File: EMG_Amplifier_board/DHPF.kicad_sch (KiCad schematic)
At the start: 7 parts, among them U4 TLV8542DR

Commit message: add footprints
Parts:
- C1, C2: footprint (none) -> Capacitor_SMD:C_0805_2012Metric
- R6, R7, R8, R9: footprint (none) -> Capacitor_SMD:C_0201_0603Metric
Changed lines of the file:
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@@
 			)
 		)
-		(property "Footprint" ""
+		(property "Footprint" "Capacitor_SMD:C_0201_0603Metric"
 			(at 116.332 101.6 90)
 			(effects
@@
 			)
 		)
-		(property "Footprint" ""
+		(property "Footprint" "Capacitor_SMD:C_0805_2012Metric"
 			(at 113.03 62.5348 0)
 			(effects
@@
 			)
 		)
-		(property "Footprint" ""
+		(property "Footprint" "Capacitor_SMD:C_0201_0603Metric"
 			(at 97.282 101.6 90)
 			(effects
@@
 			)
 		)
-		(property "Footprint" ""
+		(property "Footprint" "Capacitor_SMD:C_0805_2012Metric"
 			(at 113.03 113.3348 0)
 			(effects
@@
 			)
 		)
-		(property "Footprint" ""
+		(property "Footprint" "Capacitor_SMD:C_0201_0603Metric"
 			(at 97.282 74.93 90)
 			(effects
@@
 			)
 		)
-		(property "Footprint" ""
+		(property "Footprint" "Capacitor_SMD:C_0201_0603Metric"
 			(at 116.332 74.93 90)
 			(effects

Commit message: acomponents choice
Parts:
- C1, C2: footprint Capacitor_SMD:C_0805_2012Metric -> Capacitor_SMD:C_0603_1608Metric
- R6, R7, R8, R9: footprint Capacitor_SMD:C_0201_0603Metric -> Resistor_SMD:R_0402_1005Metric
- U4: footprint RUG8_TEX -> TLV8542DR_footprints:RUG8_TEX
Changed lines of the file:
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@@
 			)
 		)
-		(property "Footprint" "RUG8_TEX"
+		(property "Footprint" "TLV8542DR_footprints:RUG8_TEX"
 			(at 64.77 66.04 0)
 			(effects
@@
 			)
 		)
-		(property "Footprint" "Capacitor_SMD:C_0201_0603Metric"
+		(property "Footprint" "Resistor_SMD:R_0402_1005Metric"
 			(at 116.332 101.6 90)
 			(effects
@@
 			)
 		)
-		(property "Footprint" "Capacitor_SMD:C_0805_2012Metric"
+		(property "Footprint" "Capacitor_SMD:C_0603_1608Metric"
 			(at 113.03 62.5348 0)
 			(effects
@@
 			)
 		)
-		(property "Footprint" "Capacitor_SMD:C_0201_0603Metric"
+		(property "Footprint" "Resistor_SMD:R_0402_1005Metric"
 			(at 97.282 101.6 90)
 			(effects
@@
 			)
 		)
-		(property "Footprint" "Capacitor_SMD:C_0805_2012Metric"
+		(property "Footprint" "Capacitor_SMD:C_0603_1608Metric"
 			(at 113.03 113.3348 0)
 			(effects
@@
 			)
 		)
-		(property "Footprint" "Capacitor_SMD:C_0201_0603Metric"
+		(property "Footprint" "Resistor_SMD:R_0402_1005Metric"
 			(at 97.282 74.93 90)
 			(effects
@@
 			)
 		)
-		(property "Footprint" "Capacitor_SMD:C_0201_0603Metric"
+		(property "Footprint" "Resistor_SMD:R_0402_1005Metric"
 			(at 116.332 74.93 90)
 			(effects

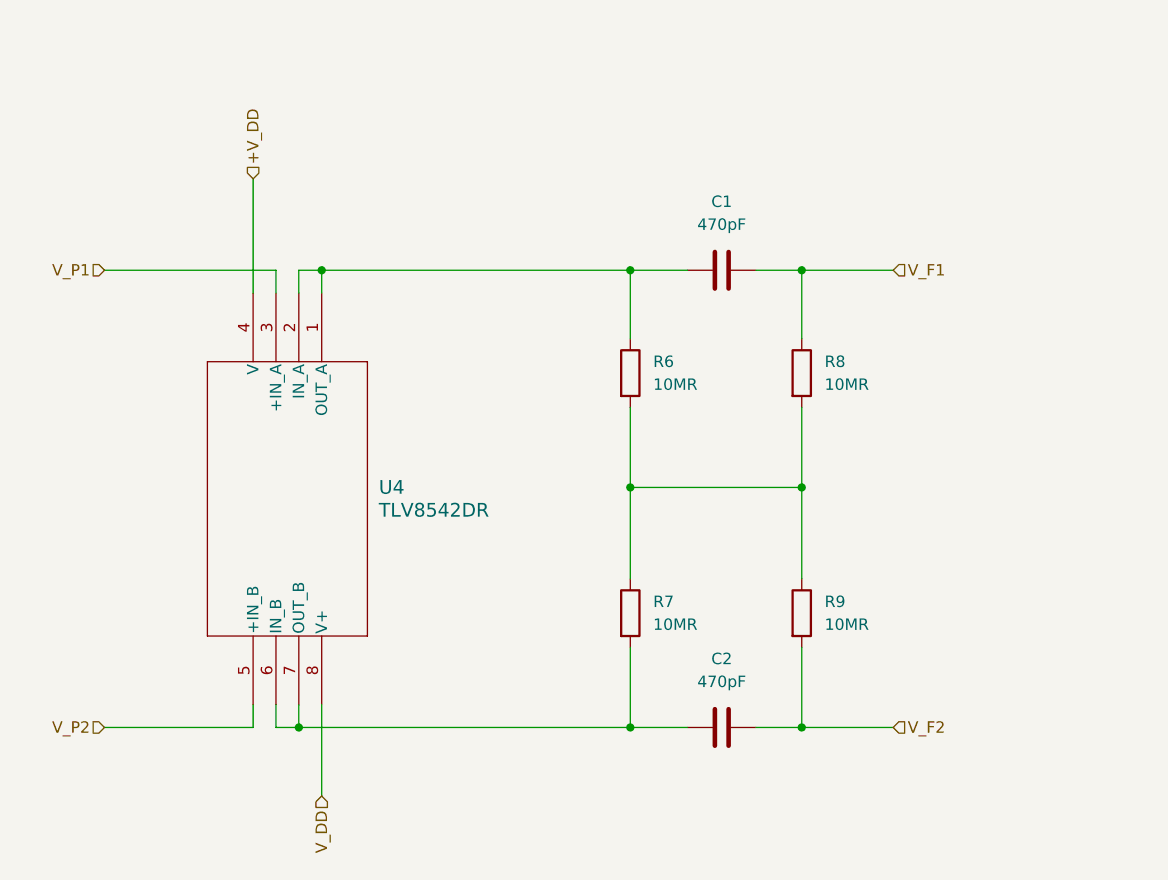
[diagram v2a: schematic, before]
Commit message: update the schematic with shared grounds and pin connectors
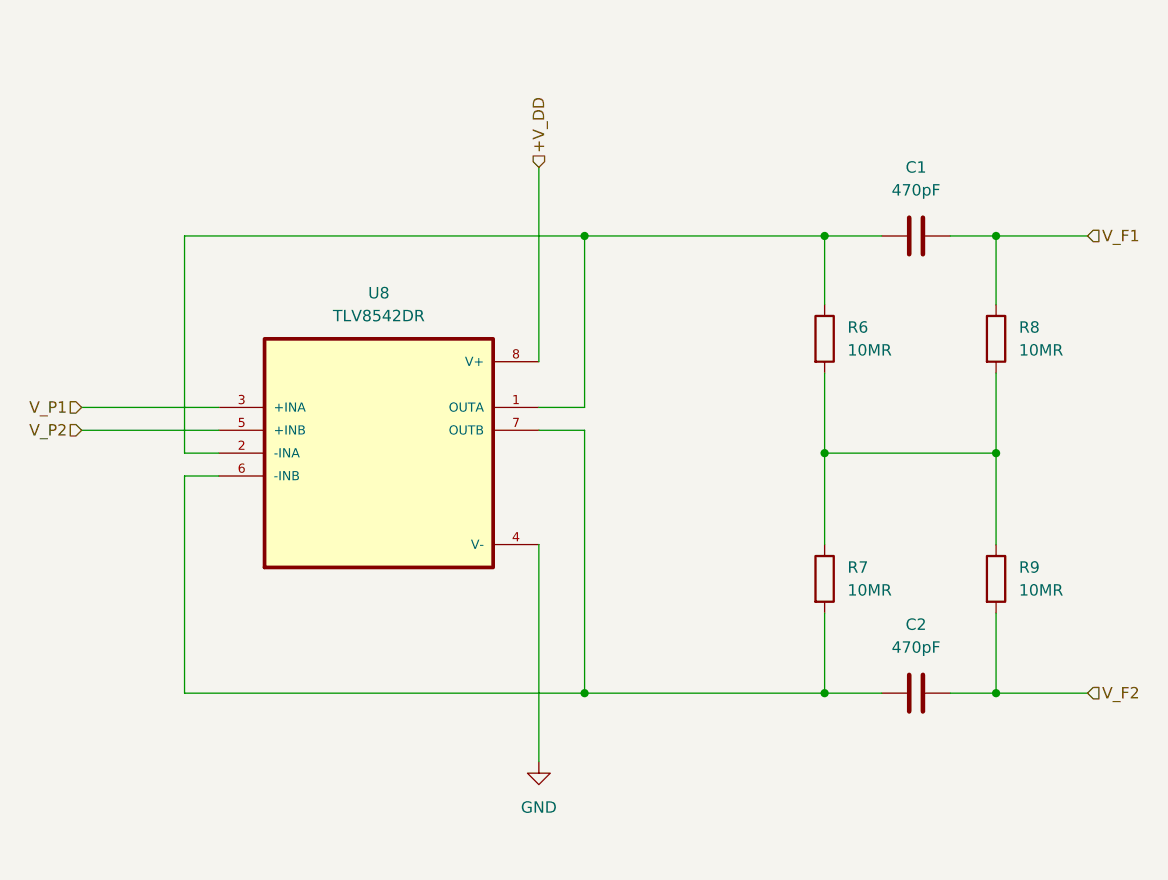
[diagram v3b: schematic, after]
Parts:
- removed U4: TLV8542DR, TLV8542DR_footprints:RUG8_TEX, symbol TLV8542DR:TLV8542DR
- added U8: TLV8542DR, TLV8542DR:SOIC127P599X175-8N, symbol TLV8542DR:TLV8542DR
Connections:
- net +V_DD: now also U8.8 (V+)
- net V_P1: now also U8.3 (+INA)
- net V_P2: now also U8.5 (+INB)
- net at C1.1, R6.1: now also U8.1 (OUTA), U8.2 (-INA)
- net at C2.1, R7.2: now also U8.6 (-INB), U8.7 (OUTB)
- new net GND: U8.4 (V-)
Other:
- moved on the sheet: C1, C2, R6, R7, R8, R9

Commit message: pcb design v1
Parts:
- added C7: 0.1uF, Capacitor_SMD:C_0805_2012Metric, symbol Device:C_Small
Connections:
- net +V_DD: now also C7.2
- net GND: now also C7.1
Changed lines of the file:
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@@
+	)
+	(junction
+		(at 88.9 50.8)
+		(diameter 0)
+		(color 0 0 0 0)
 	)
 	(junction
@@
 	(wire
 		(pts
-			(xy 88.9 52.07) (xy 88.9 73.66)
+			(xy 88.9 44.45) (xy 88.9 50.8)
 		)
 		(stroke
@@
 	(wire
 		(pts
+			(xy 77.47 50.8) (xy 73.66 50.8)
+		)
+		(stroke
+			(width 0)
+			(type default)
+		)
+	)
+	(wire
+		(pts
 			(xy 38.1 78.74) (xy 53.34 78.74)
 		)
@@
 	(wire
 		(pts
+			(xy 82.55 50.8) (xy 88.9 50.8)
+		)
+		(stroke
+			(width 0)
+			(type default)
+		)
+	)
+	(wire
+		(pts
 			(xy 134.62 110.49) (xy 139.7 110.49)
 		)
@@
 		(pts
 			(xy 120.65 83.82) (xy 139.7 83.82)
+		)
+		(stroke
+			(width 0)
+			(type default)
+		)
+	)
+	(wire
+		(pts
+			(xy 88.9 50.8) (xy 88.9 73.66)
 		)
 		(stroke
@@
 	(hierarchical_label "+V_DD"
 		(shape input)
-		(at 88.9 52.07 90)
+		(at 88.9 44.45 90)
 		(fields_autoplaced yes)
 		(effects
@@
 					(unit 1)
 				)
+			)
+		)
+	)
+	(symbol
+		(lib_id "Device:C_Small")
+		(at 80.01 50.8 90)
+		(unit 1)
+		(exclude_from_sim no)
+		(in_bom yes)
+		(on_board yes)
+		(dnp no)
+		(fields_autoplaced yes)
+		(property "Reference" "C7"
+			(at 80.0163 44.45 90)
+			(effects
+				(font
+					(size 1.27 1.27)
+				)
+			)
+		)
+		(property "Value" "0.1uF"
+			(at 80.0163 46.99 90)
+			(effects
+				(font
+					(size 1.27 1.27)
+				)
+			)
+		)
+		(property "Footprint" "Capacitor_SMD:C_0805_2012Metric"
+			(at 80.01 50.8 0)
+			(effects
+				(font
+					(size 1.27 1.27)
+				)
+				(hide yes)
+			)
+		)
+		(property "Datasheet" "~"
+			(at 80.01 50.8 0)
+			(effects
+				(font
+					(size 1.27 1.27)
+				)
+				(hide yes)
+			)
+		)
+		(property "Description" "Unpolarized capacitor, small symbol"
+			(at 80.01 50.8 0)
+			(effects
+				(font
+					(size 1.27 1.27)
+				)
+				(hide yes)
+			)
+		)
+		(pin "2"
+		)
+		(pin "1"
+		)
+		(instances
+			(project ""
+				(path "/26861adc-1ddf-4c37-9f8b-8db1c0839771/566a5450-97e0-4bc1-8c47-b0ac1397ab98/51c73326-32f2-420f-8877-30851f8c154d"
+					(reference "C7")
+					(unit 1)
+				)
+			)
+		)
+	)
+	(symbol
+		(lib_id "power:GND")
+		(at 73.66 50.8 270)
+		(unit 1)
+		(exclude_from_sim no)
+		(in_bom yes)
+		(on_board yes)
+		(dnp no)
+		(fields_autoplaced yes)
+		(property "Reference" "#PWR05"
+			(at 67.31 50.8 0)
+			(effects
+				(font
+					(size 1.27 1.27)
+				)
+				(hide yes)
+			)
+		)
+		(property "Value" "GND"
+			(at 69.85 50.7999 90)
+			(effects
+				(font
+					(size 1.27 1.27)
+				)
+				(justify right)
+			)
+		)
+		(property "Footprint" ""
+			(at 73.66 50.8 0)
+			(effects
+				(font
+					(size 1.27 1.27)
+				)
+				(hide yes)
+			)
+		)
+		(property "Datasheet" ""
+			(at 73.66 50.8 0)
+			(effects
+				(font
+					(size 1.27 1.27)
+				)
+				(hide yes)
+			)
+		)
+		(property "Description" "Power symbol creates a global label with name \"GND\" , ground"
+			(at 73.66 50.8 0)
+			(effects
+				(font
+					(size 1.27 1.27)
+				)
+				(hide yes)
+			)
+		)
+		(pin "1"
+		)
+		(instances
+			(project ""
+				(path "/26861adc-1ddf-4c37-9f8b-8db1c0839771/566a5450-97e0-4bc1-8c47-b0ac1397ab98/51c73326-32f2-420f-8877-30851f8c154d"
+					(reference "#PWR05")
+					(unit 1)
+				)

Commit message: first revision
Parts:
- R6, R7, R8, R9: value 10MR -> 10M
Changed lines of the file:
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@@
 			)
 		)
-		(property "Value" "10MR"
+		(property "Value" "10M"
 			(at 142.24 99.0599 0)
 			(effects
@@
 			)
 		)
-		(property "Value" "10MR"
+		(property "Value" "10M"
 			(at 123.19 99.0599 0)
 			(effects
@@
 			)
 		)
-		(property "Value" "10MR"
+		(property "Value" "10M"
 			(at 123.19 72.3899 0)
 			(effects
@@
 			)
 		)
-		(property "Value" "10MR"
+		(property "Value" "10M"
 			(at 142.24 72.3899 0)
 			(effects

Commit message: update R and C refs to correspond to paper
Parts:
- renumbered C7 to C20
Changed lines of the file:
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@@
 		(dnp no)
 		(fields_autoplaced yes)
-		(property "Reference" "C7"
+		(property "Reference" "C20"
 			(at 80.0163 44.45 90)
 			(effects
@@
 			(project ""
 				(path "/26861adc-1ddf-4c37-9f8b-8db1c0839771/566a5450-97e0-4bc1-8c47-b0ac1397ab98/51c73326-32f2-420f-8877-30851f8c154d"
-					(reference "C7")
+					(reference "C20")
 					(unit 1)
 				)

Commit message: replace 2012 capacitors with 1005
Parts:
- C20: footprint Capacitor_SMD:C_0805_2012Metric -> Capacitor_SMD:C_0402_1005Metric
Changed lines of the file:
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@@
 			)
 		)
-		(property "Footprint" "Capacitor_SMD:C_0805_2012Metric"
+		(property "Footprint" "Capacitor_SMD:C_0402_1005Metric"
 			(at 80.01 50.8 0)
 			(effects
